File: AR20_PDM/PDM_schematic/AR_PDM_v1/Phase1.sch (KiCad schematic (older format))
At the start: 12 parts, among them Q1 BTS50025-1TAD, U2 INA233

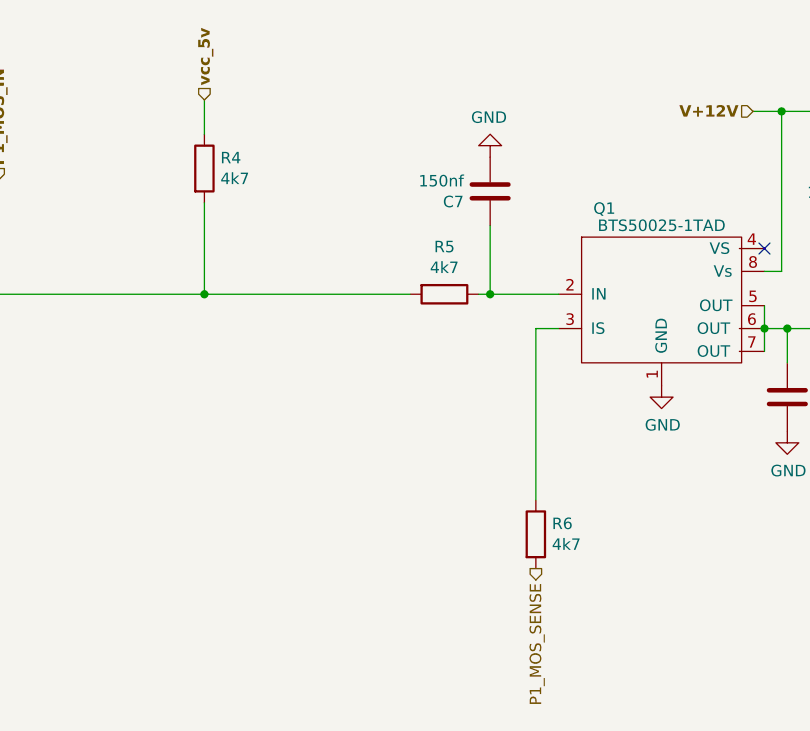
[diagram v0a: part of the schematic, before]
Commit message: Fixed wrong resistors, mos sense. Gerber files updated
- removed all R_is_protection resistors on each mosfet line
- added one R_is_protection resistors to mos_sense_all
ps, mux N-fets, does not need overvoltage protection. 60 volt tolerant.
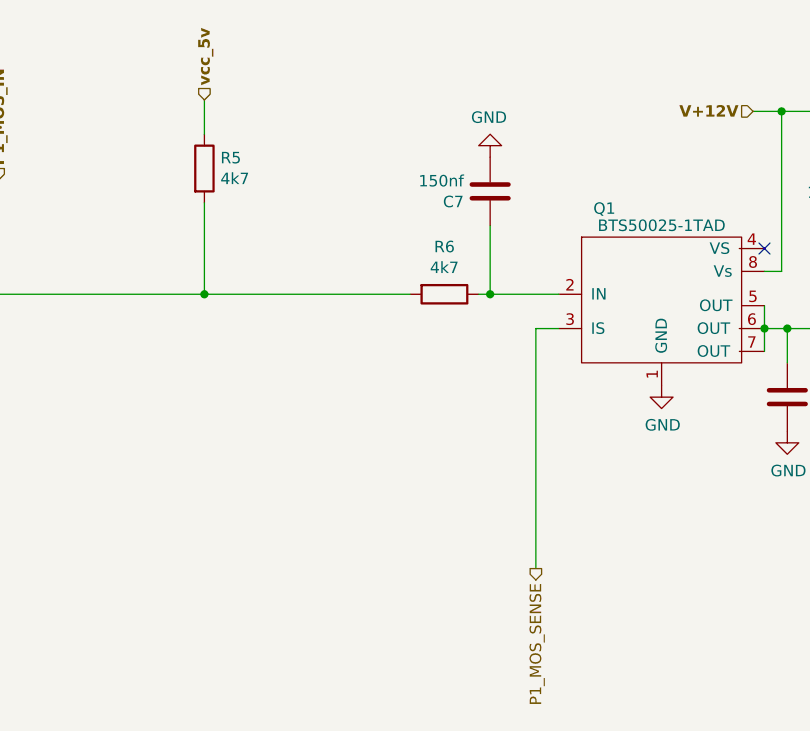
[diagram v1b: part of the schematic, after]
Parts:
- removed R6: 4k7, Resistor_SMD:R_0603_1608Metric, symbol AR20_PDM_v1-rescue:R-Device
- renumbered R4 to R5, R5 to R6
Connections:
- net P1_MOS_SENSE: now also Q1.3 (IS)
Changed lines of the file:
@@
 $EndDescr
 $Comp
-L AR20_PDM_v1-rescue:R-Device R5
+L AR20_PDM_v1-rescue:R-Device R6
 U 1 1 5E21B807
 P 3300 2400
-AR Path="/5DA89415/5E21B807" Ref="R5"  Part="1"
+AR Path="/5DA89415/5E21B807" Ref="R6"  Part="1"
 AR Path="/5DEB10A1/5E21B807" Ref="R?"  Part="1"
 AR Path="/5DEB20EA/5E21B807" Ref="R?"  Part="1"
@@
 AR Path="/5E0FDCCC/5E21B807" Ref="R?"  Part="1"
 AR Path="/5E10174B/5E21B807" Ref="R?"  Part="1"
-F 0 "R5" V 3093 2400 50  0000 C CNN
+F 0 "R6" V 3093 2400 50  0000 C CNN
 F 1 "4k7" V 3184 2400 50  0000 C CNN
 F 2 "Resistor_SMD:R_0603_1608Metric" V 3230 2400 50  0001 C CNN
@@
 $EndComp
 $Comp
-L AR20_PDM_v1-rescue:R-Device R4
+L AR20_PDM_v1-rescue:R-Device R5
 U 1 1 5E21B81B
 P 2250 1850
-AR Path="/5DA89415/5E21B81B" Ref="R4"  Part="1"
+AR Path="/5DA89415/5E21B81B" Ref="R5"  Part="1"
 AR Path="/5DEB10A1/5E21B81B" Ref="R?"  Part="1"
 AR Path="/5DEB20EA/5E21B81B" Ref="R?"  Part="1"
@@
 AR Path="/5E0FDCCC/5E21B81B" Ref="R?"  Part="1"
 AR Path="/5E10174B/5E21B81B" Ref="R?"  Part="1"
-F 0 "R4" H 2320 1896 50  0000 L CNN
+F 0 "R5" H 2320 1896 50  0000 L CNN
 F 1 "4k7" H 2320 1805 50  0000 L CNN
 F 2 "Resistor_SMD:R_0603_1608Metric" V 2180 1850 50  0001 C CNN
@@
 Wire Wire Line
 	6000 4100 8750 4100
-$Comp
-L AR20_PDM_v1-rescue:R-Device R6
-U 1 1 5E21B875
-P 3700 3450
-AR Path="/5DA89415/5E21B875" Ref="R6"  Part="1"
-AR Path="/5DEB10A1/5E21B875" Ref="R?"  Part="1"
-AR Path="/5DEB20EA/5E21B875" Ref="R?"  Part="1"
-AR Path="/5E0E4725/5E21B875" Ref="R?"  Part="1"
-AR Path="/5E0E4A93/5E21B875" Ref="R?"  Part="1"
-AR Path="/5E0E4EB5/5E21B875" Ref="R?"  Part="1"
-AR Path="/5E0E5304/5E21B875" Ref="R?"  Part="1"
-AR Path="/5E0E594B/5E21B875" Ref="R?"  Part="1"
-AR Path="/5E0E607C/5E21B875" Ref="R?"  Part="1"
-AR Path="/5E0FB5C8/5E21B875" Ref="R?"  Part="1"
-AR Path="/5E0FBBBD/5E21B875" Ref="R?"  Part="1"
-AR Path="/5E0FC3A2/5E21B875" Ref="R?"  Part="1"
-AR Path="/5E0FCFDC/5E21B875" Ref="R?"  Part="1"
-AR Path="/5E0FDCCC/5E21B875" Ref="R?"  Part="1"
-AR Path="/5E10174B/5E21B875" Ref="R?"  Part="1"
-F 0 "R6" H 3770 3496 50  0000 L CNN
-F 1 "4k7" H 3770 3405 50  0000 L CNN
-F 2 "Resistor_SMD:R_0603_1608Metric" V 3630 3450 50  0001 C CNN
-F 3 "~" H 3700 3450 50  0001 C CNN
-	1    3700 3450
-	1    0    0    -1
-$EndComp
 Wire Wire Line
 	6325 4400 8750 4400
@@
 Wire Wire Line
 	6000 2950 6325 2950
-Wire Wire Line
-	3700 2550 3700 3300
 Connection ~ 4775 1600
 Wire Wire Line
@@
 	4775 1600 4775 2300
 NoConn ~ 4700 2200
+Wire Wire Line
+	3700 2550 3700 3600
 $EndSCHEMATC

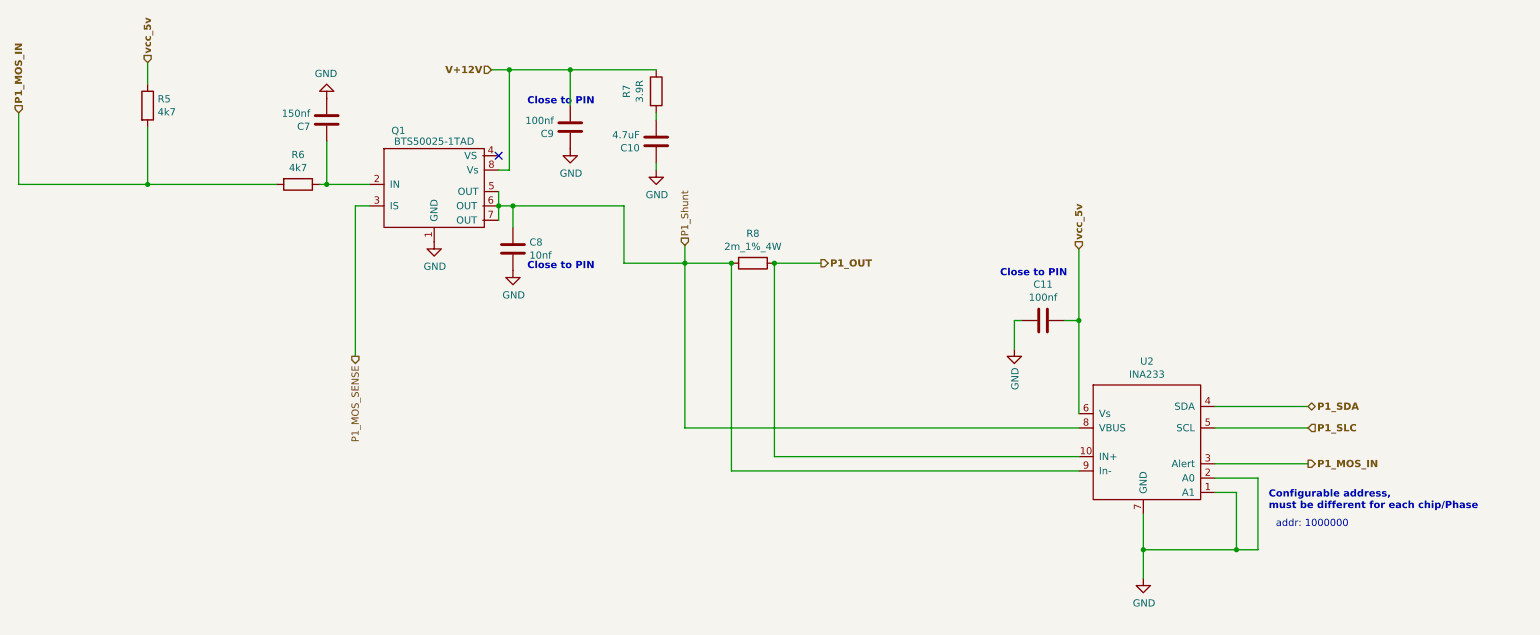
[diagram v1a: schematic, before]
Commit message: Major redesign. schematics completed, PCB work in progress
-TODO : A proper changelog file. Where all changes will apear 
- Redesigned schematics to accommodate errors in the improvement list
- More detail in ALPHA improvement list
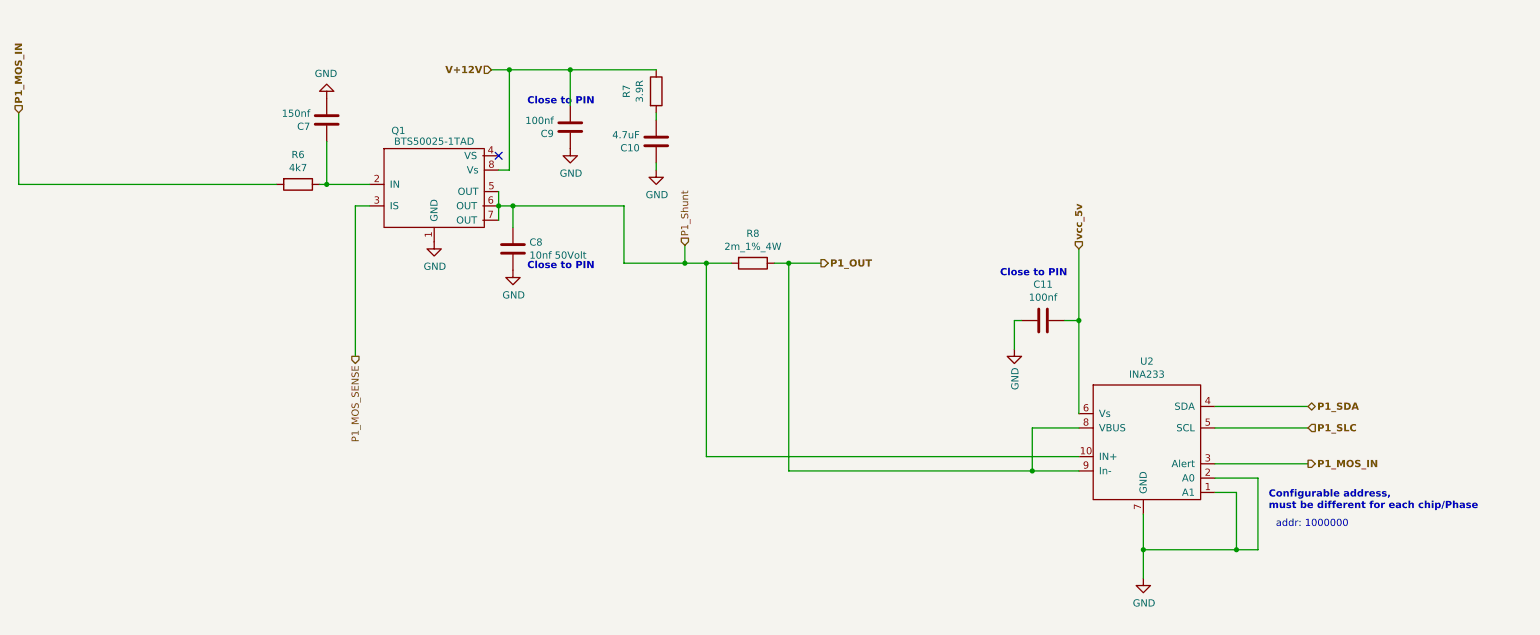
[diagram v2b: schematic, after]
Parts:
- removed R5: 4k7, Resistor_SMD:R_0603_1608Metric, symbol AR20_PDM_v1-rescue:R-Device
- C8: value 10nf -> 10nf 50Volt
- R7: footprint Resistor_SMD:R_0603_1608Metric -> Resistor_SMD:R_2512_6332Metric
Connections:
- net P1_OUT: now also U2.8 (VBUS), U2.9 (In-); no longer U2.10 (IN+)
- net P1_Shunt: now also U2.10 (IN+); no longer U2.8 (VBUS), U2.9 (In-)
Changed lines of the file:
@@
 $Descr A4 11693 8268
 encoding utf-8
-Sheet 2 13
+Sheet 2 14
 Title ""
 Date ""
@@
 AR Path="/5E10174B/5E21B80F" Ref="C?"  Part="1"
 F 0 "C8" H 4915 2896 50  0000 L CNN
-F 1 "10nf" H 4915 2805 50  0000 L CNN
+F 1 "10nf 50Volt" H 4915 2805 50  0000 L CNN
 F 2 "Capacitor_SMD:C_0603_1608Metric" H 4838 2700 50  0001 C CNN
 F 3 "~" H 4800 2850 50  0001 C CNN
@@
 $EndComp
 $Comp
-L AR20_PDM_v1-rescue:R-Device R5
-U 1 1 5E21B81B
-P 2250 1850
-AR Path="/5DA89415/5E21B81B" Ref="R5"  Part="1"
-AR Path="/5DEB10A1/5E21B81B" Ref="R?"  Part="1"
-AR Path="/5DEB20EA/5E21B81B" Ref="R?"  Part="1"
-AR Path="/5E0E4725/5E21B81B" Ref="R?"  Part="1"
-AR Path="/5E0E4A93/5E21B81B" Ref="R?"  Part="1"
-AR Path="/5E0E4EB5/5E21B81B" Ref="R?"  Part="1"
-AR Path="/5E0E5304/5E21B81B" Ref="R?"  Part="1"
-AR Path="/5E0E594B/5E21B81B" Ref="R?"  Part="1"
-AR Path="/5E0E607C/5E21B81B" Ref="R?"  Part="1"
-AR Path="/5E0FB5C8/5E21B81B" Ref="R?"  Part="1"
-AR Path="/5E0FBBBD/5E21B81B" Ref="R?"  Part="1"
-AR Path="/5E0FC3A2/5E21B81B" Ref="R?"  Part="1"
-AR Path="/5E0FCFDC/5E21B81B" Ref="R?"  Part="1"
-AR Path="/5E0FDCCC/5E21B81B" Ref="R?"  Part="1"
-AR Path="/5E10174B/5E21B81B" Ref="R?"  Part="1"
-F 0 "R5" H 2320 1896 50  0000 L CNN
-F 1 "4k7" H 2320 1805 50  0000 L CNN
-F 2 "Resistor_SMD:R_0603_1608Metric" V 2180 1850 50  0001 C CNN
-F 3 "~" H 2250 1850 50  0001 C CNN
-	1    2250 1850
-	1    0    0    -1
-$EndComp
-$Comp
 L AR20_PDM_v1-rescue:C-Device C11
 U 1 1 5E21B828
@@
 Text Notes 8200 3050 0    50   ~ 10
 Close to PIN
-Text HLabel 2250 1550 1    50   Input ~ 10
-vcc_5v
 Wire Wire Line
 	9700 4100 10350 4100
-Wire Wire Line
-	2250 1550 2250 1700
 $Comp
 L AR20_PDM_v1-rescue:C-Device C9
@@
 F 0 "R7" V 5593 1750 50  0000 C CNN
 F 1 "3.9R" V 5684 1750 50  0000 C CNN
-F 2 "Resistor_SMD:R_0603_1608Metric" V 5730 1750 50  0001 C CNN
+F 2 "Resistor_SMD:R_2512_6332Metric" V 5730 1750 50  0001 C CNN
 F 3 "~" H 5800 1750 50  0001 C CNN
 	1    5800 1750
@@
 Wire Wire Line
 	9700 4350 10350 4350
-Connection ~ 2250 2400
-Wire Wire Line
-	2250 2000 2250 2400
 Wire Wire Line
 	1350 1900 1350 2400
-Wire Wire Line
-	1350 2400 2250 2400
 Wire Wire Line
 	9200 4950 9200 5150
@@
 	5575 2550 5575 2950
 Connection ~ 4800 2550
-Wire Wire Line
-	6000 4100 8750 4100
-Wire Wire Line
-	6325 4400 8750 4400
-Wire Wire Line
-	6625 4300 8750 4300
 Text HLabel 3700 3600 3    50   Output ~ 0
 P1_MOS_SENSE
-Wire Wire Line
-	6000 4100 6000 2950
 Wire Wire Line
 	5575 2950 6000 2950
@@
 Text HLabel 4650 1600 0    50   Input ~ 10
 V+12V
-Wire Wire Line
-	2250 2400 3150 2400
-Wire Wire Line
-	6625 2950 6625 4300
-Wire Wire Line
-	6325 2950 6325 4400
 $Comp
 L AR20_PDM_v1-rescue:R-Device R8
@@
 $EndComp
 Wire Wire Line
-	6625 2950 6950 2950
-Connection ~ 6325 2950
-Connection ~ 6625 2950
+	6625 2950 6725 2950
 Text Notes 10125 4800 0    50   ~ 0
 addr: 1000000
@@
 Connection ~ 6000 2950
 Wire Wire Line
-	6000 2950 6325 2950
+	6000 2950 6150 2950
 Connection ~ 4775 1600
 Wire Wire Line
@@
 Wire Wire Line
 	3700 2550 3700 3600
+Wire Wire Line
+	1350 2400 3150 2400
+Wire Wire Line
+	8750 4300 6150 4300
+Wire Wire Line
+	6150 4300 6150 2950
+Connection ~ 6150 2950
+Wire Wire Line
+	6150 2950 6325 2950
+Wire Wire Line
+	8750 4400 8425 4400
+Wire Wire Line
+	6725 4400 6725 2950
+Connection ~ 6725 2950
+Wire Wire Line
+	6725 2950 6950 2950
+Wire Wire Line
+	8750 4100 8425 4100
+Wire Wire Line
+	8425 4100 8425 4400
+Connection ~ 8425 4400
+Wire Wire Line
+	8425 4400 6725 4400
 $EndSCHEMATC

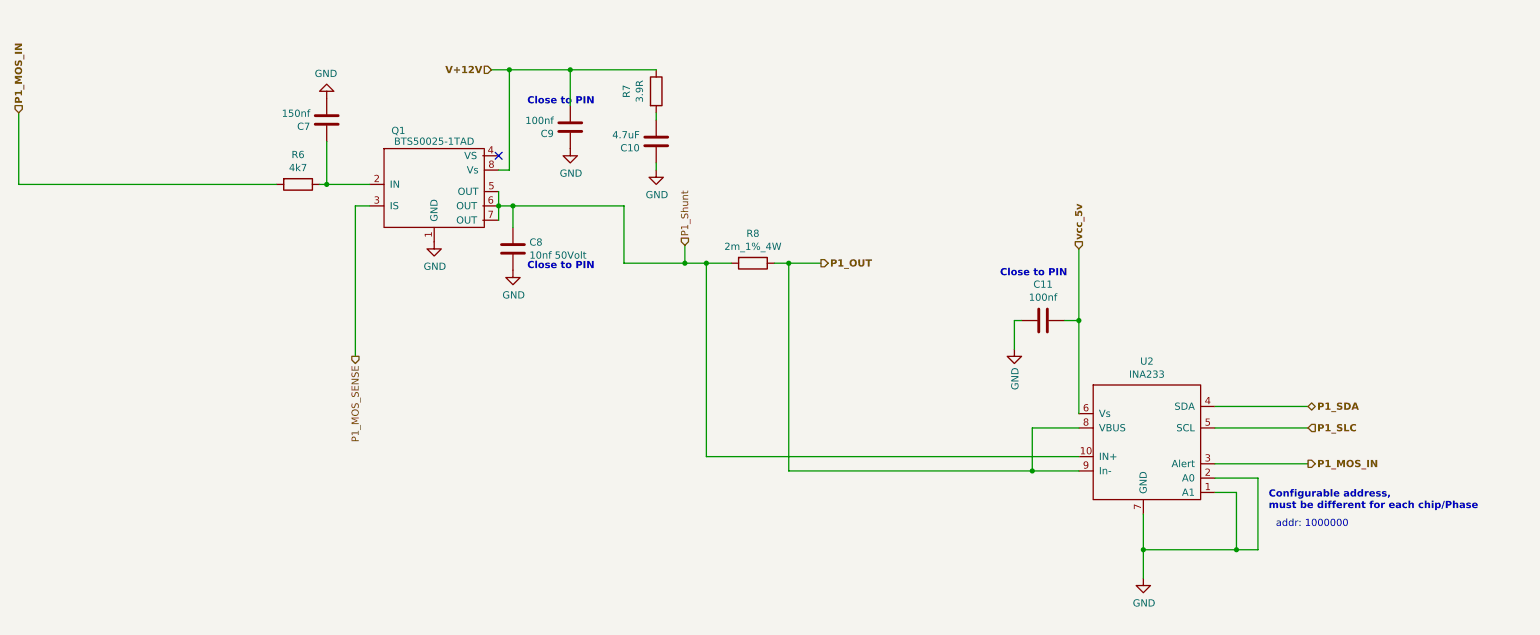
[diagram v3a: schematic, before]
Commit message: schematics rework
Fixed INA233 frying due to inductive flyback:
- Paced ina233 high side of the mosftets
- New input protection reseistors, and zener diodes, on each ina233.
Simplified:
- Removed the MUX and mos sense lines, as i realize that most of this functionality can be obtained trough INA233.
- Removed some of the cappacitors , besides the most needed ones.
- removed  back to back zener diode configuration, now a single diode insted.
 to reduce negative voltage in case of loss of VS, to be easy on the INA233 filters.
new stuff:
- Another temp sensor.
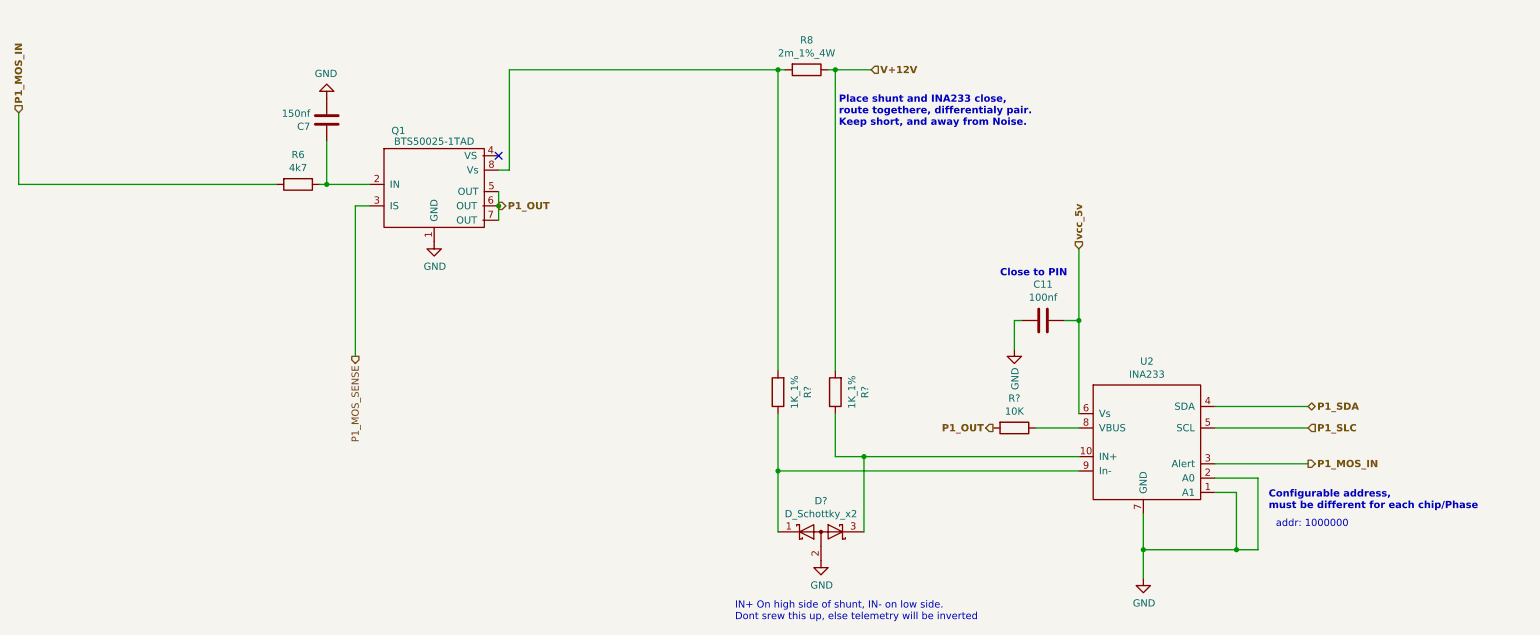
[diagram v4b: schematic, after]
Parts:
- removed C10: 4.7uF, Capacitor_SMD:C_1206_3216Metric, symbol AR20_PDM_v1-rescue:C-Device
- removed C8: 10nf 50Volt, Capacitor_SMD:C_0603_1608Metric, symbol AR20_PDM_v1-rescue:C-Device
- removed C9: 100nf, Capacitor_SMD:C_0603_1608Metric, symbol AR20_PDM_v1-rescue:C-Device
- removed R7: 3.9R, Resistor_SMD:R_2512_6332Metric, symbol AR20_PDM_v1-rescue:R-Device
- added D?: D_Schottky_x2, symbol AR20_PDM_v1-rescue:D_Schottky_x2
- added R? (x2): 1K_1%, Resistor_SMD:R_0603_1608Metric, symbol AR20_PDM_v1-rescue:R-Device
- added R?: 10K, Resistor_SMD:R_0603_1608Metric, symbol AR20_PDM_v1-rescue:R-Device
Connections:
- net GND: now also D?.2 (A)
- net P1_OUT: now also Q1.5 (OUT), Q1.6 (OUT), Q1.7 (OUT), R?.2; no longer R8.1, U2.8 (VBUS), U2.9 (In-)
- net V+12V: now also R8.1, R?.2; no longer Q1.8 (Vs)
- removed net P1_Shunt: Q1.5 (OUT), Q1.6 (OUT), Q1.7 (OUT), R8.2, U2.10 (IN+)
- new net: Q1.8 (Vs), R8.2, R?.2
- new net: D?.3 (K), R?.1, U2.10 (IN+)
- new net: R?.1, U2.8 (VBUS)
- new net: D?.1 (K), R?.1, U2.9 (In-)
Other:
- note added: "IN+ On high side of shunt, IN- on low side.\nDont srew this up, else telemetry will be inverted"
- note added: "Place shunt and INA233 close, \nroute togethere, differentialy pair. \nKeep short, and away from Noise."
- moved on the sheet: R8
